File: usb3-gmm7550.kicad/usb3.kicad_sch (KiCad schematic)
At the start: 31 parts, among them J1 USB_C_Receptacle, U1 ECMF4-40A100N10, U2 ECMF4-40A100N10, U3 ECMF02-2AMX6, U4 AP7330, U5 TUSB542

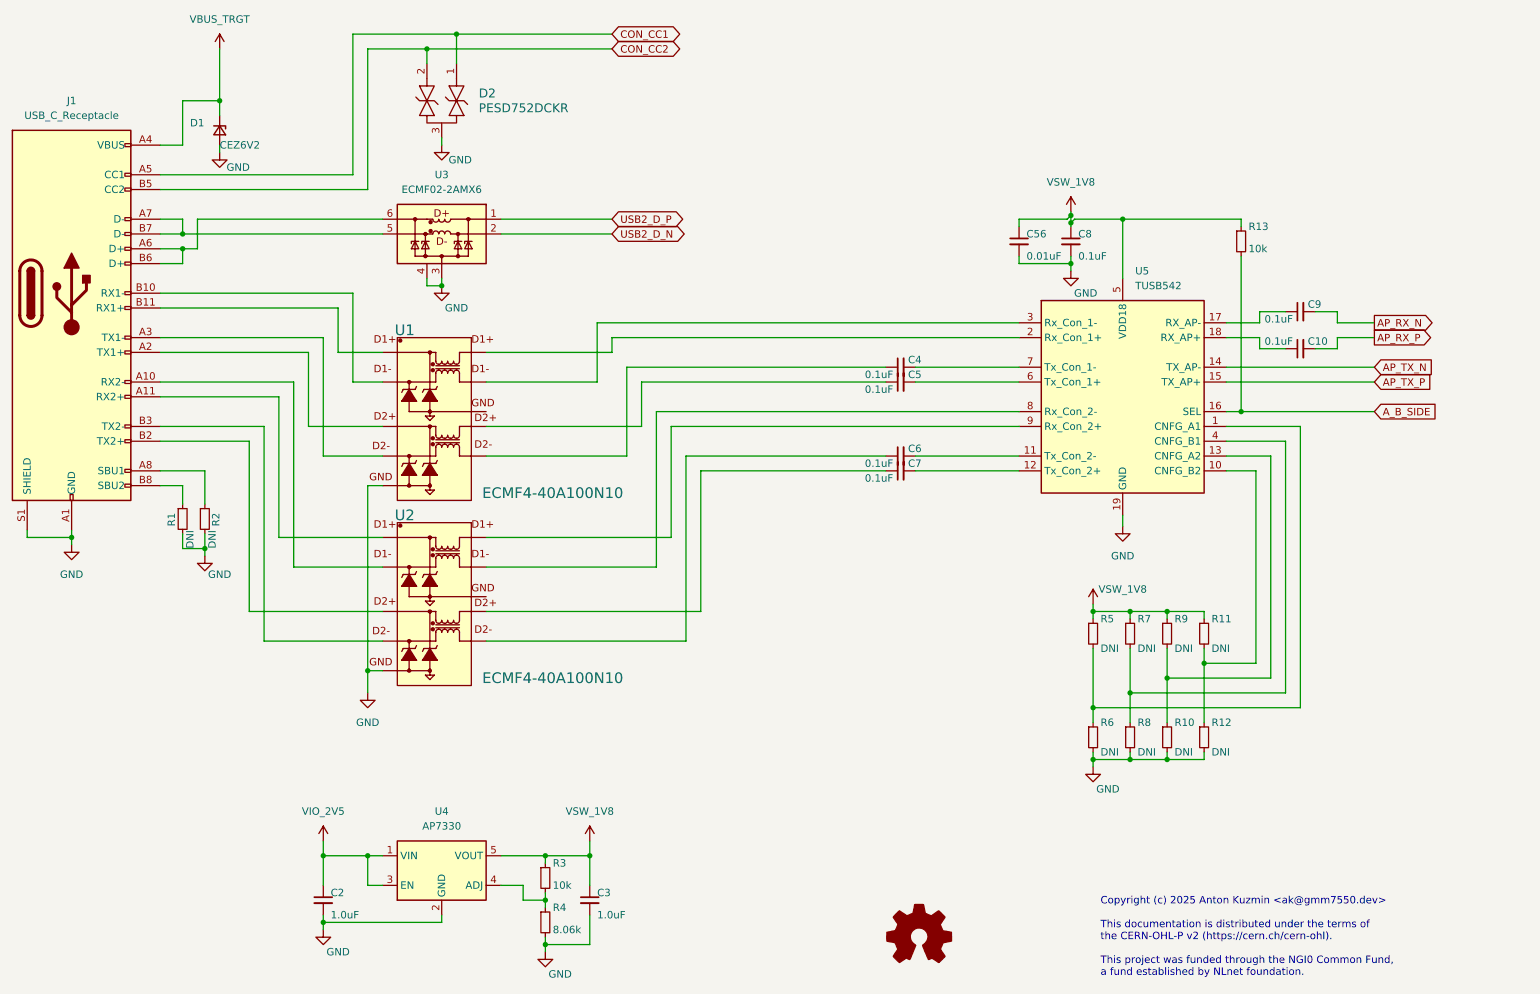
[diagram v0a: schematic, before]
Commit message: Connect USB 3 SuperSpeed diff. pairs
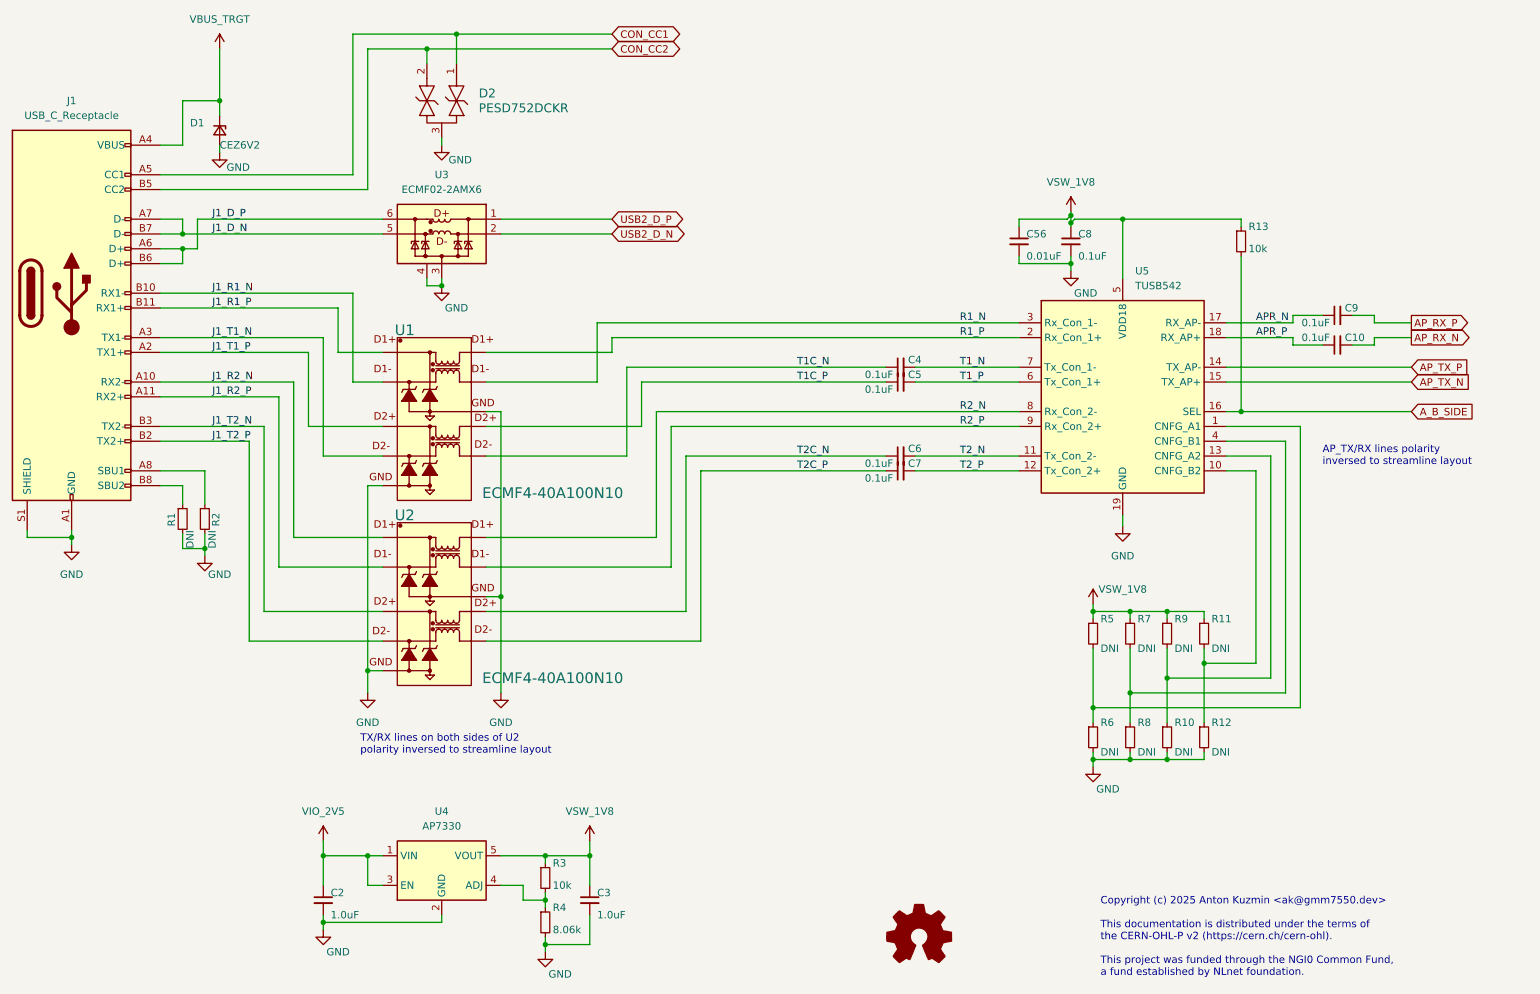
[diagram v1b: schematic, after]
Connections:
- net AP_RX_N: now also C10.2; no longer C9.2
- net AP_RX_P: now also C9.2; no longer C10.2
- net AP_TX_N: now also U5.15 (TX_AP+); no longer U5.14 (TX_AP-)
- net AP_TX_P: now also U5.14 (TX_AP-); no longer U5.15 (TX_AP+)
- net GND: now also U1.8 (GND1), U2.8 (GND1)
- net APR_N: now reaches C9.1, U5.17 (RX_AP-)
- net T1C_N: now reaches C4.1, U1.6 (D2-1)
- net T1_N: now reaches C4.2, U5.7 (Tx_Con_1-)
- net J1_R1_P: now reaches J1.B11 (RX1+), U1.1 (D1+)
- net R1_P: now reaches U1.10 (D1+1), U5.2 (Rx_Con_1+)
- net J1_R1_N: now reaches J1.B10 (RX1-), U1.2 (D1-)
- net J1_T1_P: now reaches J1.A2 (TX1+), U1.4 (D2+)
- net J1_T1_N: now reaches J1.A3 (TX1-), U1.5 (D2-)
- net T1C_P: now reaches C5.1, U1.7 (D2+1)
- net R1_N: now reaches U1.9 (D1-1), U5.3 (Rx_Con_1-)
- net J1_R2_N: now reaches U2.1 (D1+)
- net J1_R2_N: now also J1.A10 (RX2-); no longer J1.A11 (RX2+)
- net R2_N: now reaches U2.10 (D1+1)
- net R2_N: now also U5.8 (Rx_Con_2-); no longer U5.9 (Rx_Con_2+)
- net J1_R2_P: now reaches U2.2 (D1-)
- net J1_R2_P: now also J1.A11 (RX2+); no longer J1.A10 (RX2-)
- net J1_T2_N: now reaches U2.4 (D2+)
- net J1_T2_N: now also J1.B3 (TX2-); no longer J1.B2 (TX2+)
- net J1_T2_P: now reaches U2.5 (D2-)
- net J1_T2_P: now also J1.B2 (TX2+); no longer J1.B3 (TX2-)
- net T2C_N: now reaches C6.1
- net T2C_N: now also U2.7 (D2+1); no longer U2.6 (D2-1)
- net T2C_P: now reaches C7.1
- net T2C_P: now also U2.6 (D2-1); no longer U2.7 (D2+1)
- net R2_P: now reaches U2.9 (D1-1)
- net R2_P: now also U5.9 (Rx_Con_2+); no longer U5.8 (Rx_Con_2-)
- net T2_N: now reaches C6.2, U5.11 (Tx_Con_2-)
- net T2_P: now reaches C7.2, U5.12 (Tx_Con_2+)
- net APR_P: now reaches C10.1, U5.18 (RX_AP+)
- net T1_P: now reaches C5.2, U5.6 (Tx_Con_1+)
- net J1_D_N: now reaches J1.A7 (D-), J1.B7 (D-), U3.5 (D-_out)
- net J1_D_P: now reaches J1.A6 (D+), J1.B6 (D+), U3.6 (D+_out)
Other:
- note added: "AP_TX/RX lines polarity inversed to streamline layout"
- note added: "TX/RX lines on both sides of U2 polarity inversed to streamline layout"
- moved on the sheet: C10, C9

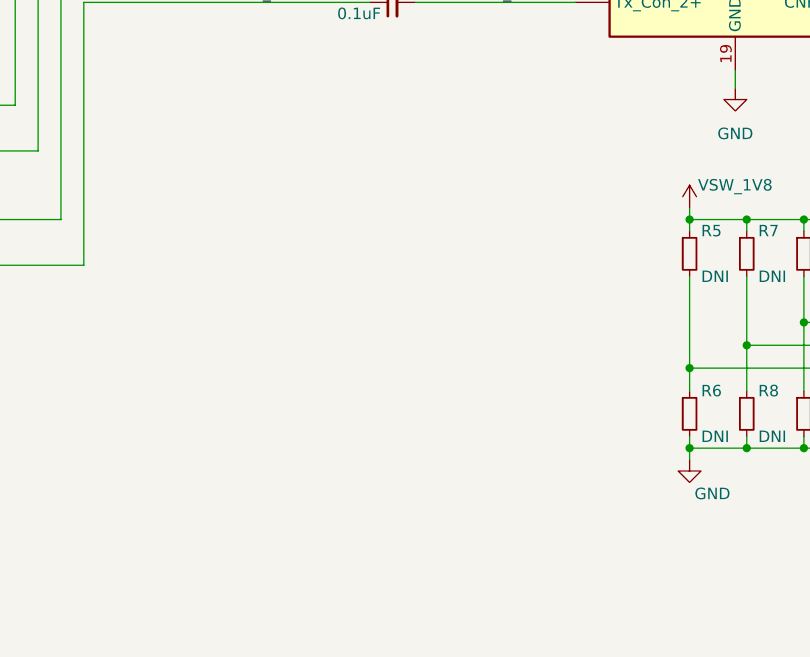
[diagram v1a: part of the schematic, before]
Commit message: Add USB Type-C plug polarity indication (A_B_SIDE signal from PD controller)
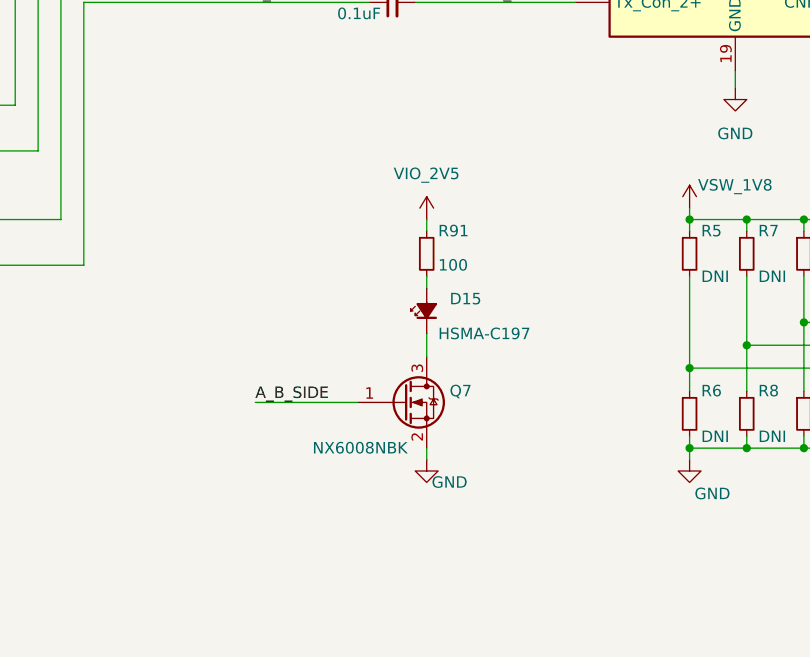
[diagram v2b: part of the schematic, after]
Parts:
- added D15: HSMA-C197, LED_SMD:LED_0603_1608Metric, symbol Device:LED_Small_Filled
- added Q7: NX6008NBK, Package_TO_SOT_SMD:SOT-23, symbol Device:Q_NMOS_GSD
- added R91: 100, Resistor_SMD:R_0402_1005Metric, symbol Device:R_Small
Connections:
- net A_B_SIDE: now also Q7.1 (G)
- net GND: now also Q7.2 (S)
- net VIO_2V5: now also R91.1
- new net: D15.1 (K), Q7.3 (D)
- new net: D15.2 (A), R91.2

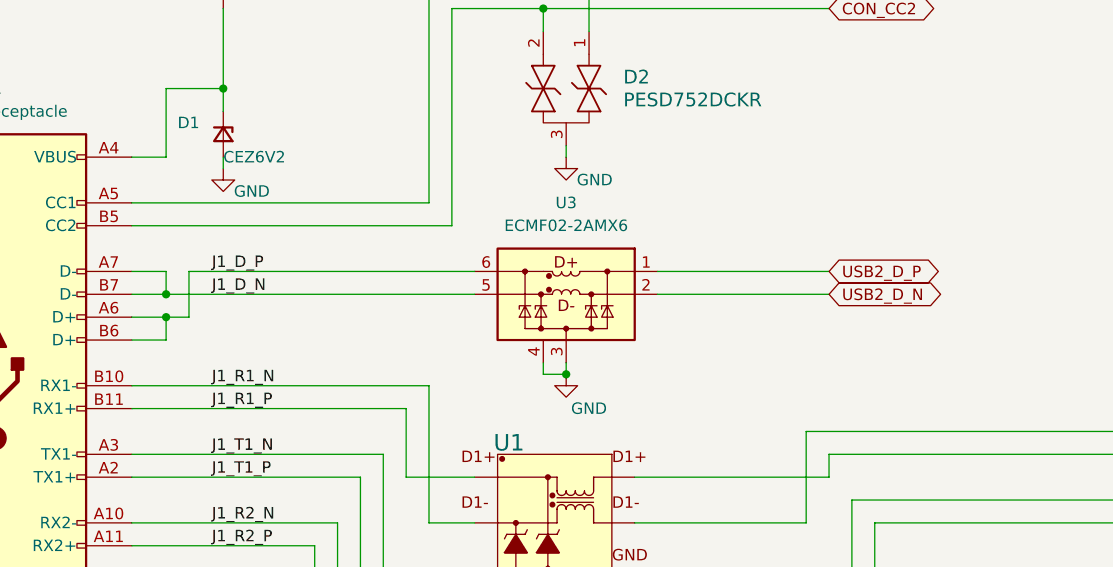
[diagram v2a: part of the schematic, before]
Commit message: Layout -- re-arrange and connect all GMM-7550 IOs on J4 (USB 1.1 and 2.0)
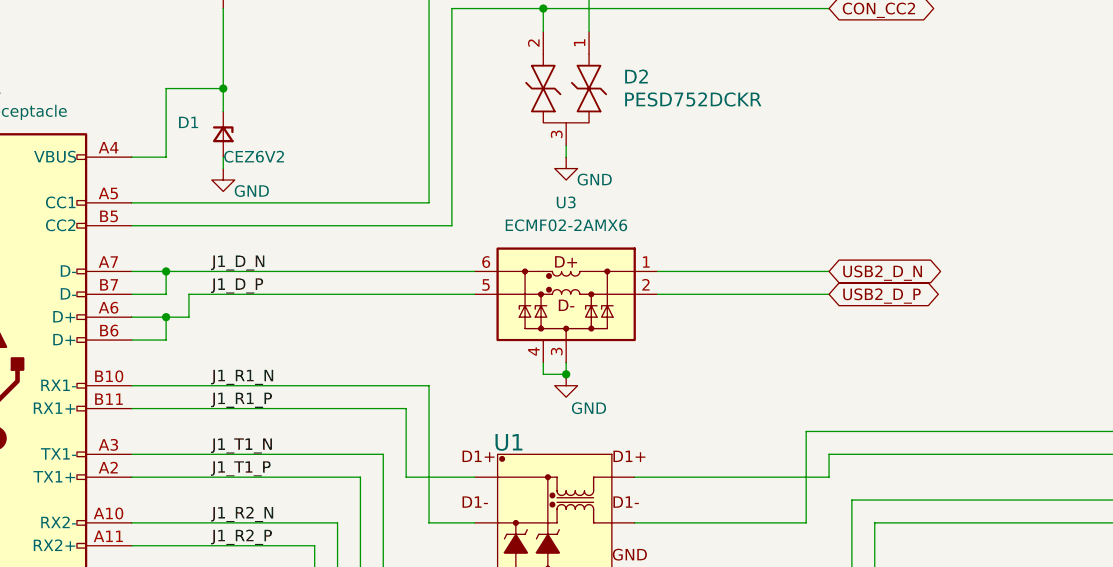
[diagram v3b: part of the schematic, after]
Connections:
- net J1_D_N: now also U3.6 (D+_out); no longer U3.5 (D-_out)
- net J1_D_P: now also U3.5 (D-_out); no longer U3.6 (D+_out)
- net USB2_D_N: now also U3.1 (D+_in); no longer U3.2 (D-_in)
- net USB2_D_P: now also U3.2 (D-_in); no longer U3.1 (D+_in)
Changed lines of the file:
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@@
 	(title_block
 		(title "GMM-7550 USB3 Adapter")
-		(date "2025-09-02")
-		(rev "0.9.3")
+		(date "2025-09-xx")
+		(rev "0.9.4")
 	)
 	(text "Copyright (c) 2025 Anton Kuzmin <ak@gmm7550.dev>\n\nThis documentation is distributed under the terms of\nthe CERN-OHL-P v2 (https://cern.ch/cern-ohl).\n\nThis project was funded through the NGI0 Common Fund,\na fund established by NLnet foundation."
@@
 	)
 	(junction
-		(at 57.15 53.34)
-		(diameter 0)
-		(color 0 0 0 0)
-	)
-	(junction
 		(at 232.41 127)
 		(diameter 0)
@@
 	)
 	(junction
+		(at 57.15 50.8)
+		(diameter 0)
+		(color 0 0 0 0)
+	)
+	(junction
 		(at 226.06 118.11)
 		(diameter 0)
@@
 	(wire
 		(pts
-			(xy 57.15 53.34) (xy 91.44 53.34)
-		)
-		(stroke
-			(width 0)
-			(type default)
-		)
-	)
-	(wire
-		(pts
 			(xy 128.27 78.74) (xy 128.27 68.58)
 		)
@@
 	(wire
 		(pts
-			(xy 111.76 50.8) (xy 130.81 50.8)
-		)
-		(stroke
-			(width 0)
-			(type default)
-		)
-	)
-	(wire
-		(pts
 			(xy 109.22 73.66) (xy 130.81 73.66)
 		)
@@
 	(wire
 		(pts
+			(xy 111.76 50.8) (xy 130.81 50.8)
+		)
+		(stroke
+			(width 0)
+			(type default)
+		)
+	)
+	(wire
+		(pts
 			(xy 236.22 91.44) (xy 243.84 91.44)
 		)
@@
 	(wire
 		(pts
-			(xy 59.69 55.88) (xy 57.15 55.88)
+			(xy 57.15 55.88) (xy 59.69 55.88)
 		)
 		(stroke
@@
 	(wire
 		(pts
-			(xy 111.76 53.34) (xy 130.81 53.34)
-		)
-		(stroke
-			(width 0)
-			(type default)
-		)
-	)
-	(wire
-		(pts
 			(xy 53.34 81.28) (xy 73.66 81.28)
 		)
@@
 	(wire
 		(pts
+			(xy 59.69 55.88) (xy 59.69 53.34)
+		)
+		(stroke
+			(width 0)
+			(type default)
+		)
+	)
+	(wire
+		(pts
 			(xy 60.96 104.775) (xy 60.96 107.315)
 		)
@@
 	(wire
 		(pts
-			(xy 78.74 73.66) (xy 78.74 86.36)
+			(xy 57.15 50.8) (xy 91.44 50.8)
 		)
 		(stroke
@@
 	(wire
 		(pts
-			(xy 86.36 78.74) (xy 91.44 78.74)
+			(xy 78.74 73.66) (xy 78.74 86.36)
 		)
 		(stroke
@@
 	(wire
 		(pts
-			(xy 99.06 60.96) (xy 99.06 62.23)
+			(xy 86.36 78.74) (xy 91.44 78.74)
 		)
 		(stroke
@@
 	(wire
 		(pts
-			(xy 88.9 165.1) (xy 88.9 160.02)
+			(xy 99.06 60.96) (xy 99.06 62.23)
 		)
 		(stroke
@@
 	(wire
 		(pts
-			(xy 53.34 53.34) (xy 57.15 53.34)
+			(xy 88.9 165.1) (xy 88.9 160.02)
 		)
 		(stroke
@@
 	(wire
 		(pts
-			(xy 182.88 78.74) (xy 200.66 78.74)
+			(xy 53.34 53.34) (xy 57.15 53.34)
 		)
 		(stroke
@@
 	(wire
 		(pts
-			(xy 209.55 51.435) (xy 209.55 52.07)
+			(xy 182.88 78.74) (xy 200.66 78.74)
 		)
 		(stroke
@@
 	(wire
 		(pts
-			(xy 59.69 50.8) (xy 59.69 55.88)
+			(xy 209.55 51.435) (xy 209.55 52.07)
 		)
 		(stroke
@@
 	(wire
 		(pts
+			(xy 59.69 53.34) (xy 91.44 53.34)
+		)
+		(stroke
+			(width 0)
+			(type default)
+		)
+	)
+	(wire
+		(pts
 			(xy 209.55 58.42) (xy 209.55 59.69)
 		)
@@
 	(wire
 		(pts
+			(xy 111.76 53.34) (xy 130.81 53.34)
+		)
+		(stroke
+			(width 0)
+			(type default)
+		)
+	)
+	(wire
+		(pts
 			(xy 210.185 50.8) (xy 209.55 51.435)
 		)
@@
 	(wire
 		(pts
-			(xy 91.44 50.8) (xy 59.69 50.8)
-		)
-		(stroke
-			(width 0)
-			(type default)
-		)
-	)
-	(wire
-		(pts
 			(xy 236.22 78.74) (xy 267.97 78.74)
 		)
@@
 	)
 	(label "J1_D_N"
-		(at 62.23 53.34 0)
+		(at 62.23 50.8 0)
 		(effects
 			(font
@@
 	)
 	(label "J1_D_P"
-		(at 62.23 50.8 0)
+		(at 62.23 53.34 0)
 		(effects
 			(font
@@
 	(global_label "USB2_D_N"
 		(shape bidirectional)
-		(at 130.81 53.34 0)
+		(at 130.81 50.8 0)
 		(fields_autoplaced yes)
 		(effects
@@
 		)
 		(property "Intersheetrefs" "${INTERSHEET_REFS}"
-			(at 144.4617 53.34 0)
+			(at 144.4617 50.8 0)
 			(effects
 				(font
@@
 	(global_label "USB2_D_P"
 		(shape bidirectional)
-		(at 130.81 50.8 0)
+		(at 130.81 53.34 0)
 		(fields_autoplaced yes)
 		(effects
@@
 		)
 		(property "Intersheetrefs" "${INTERSHEET_REFS}"
-			(at 144.4012 50.8 0)
+			(at 144.4012 53.34 0)
 			(effects
 				(font

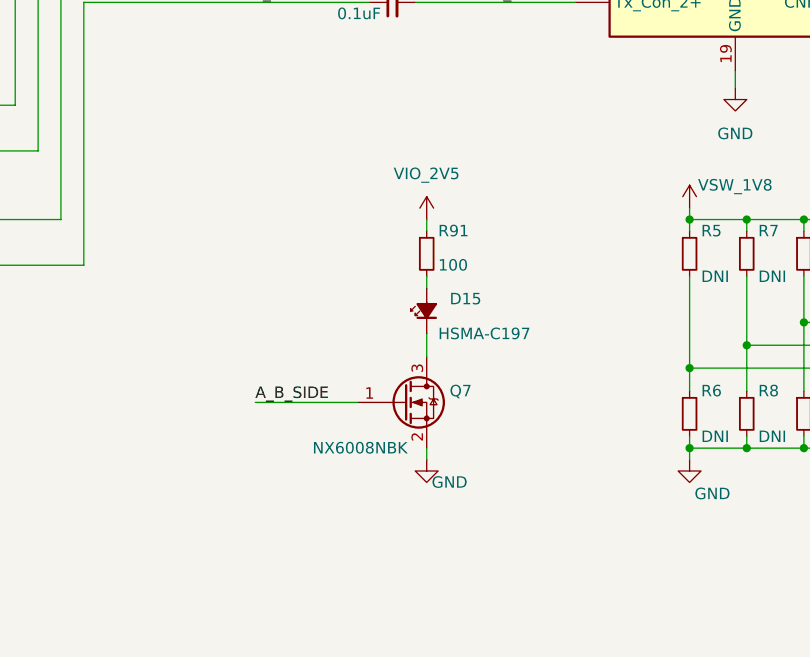
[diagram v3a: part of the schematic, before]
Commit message: USB Power Delivery redesign (STmicro controller is NRND)
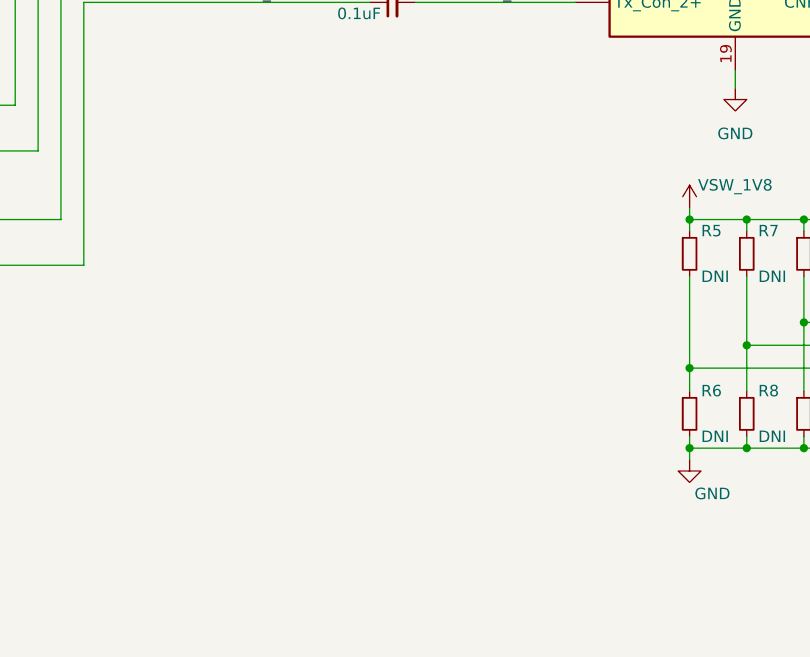
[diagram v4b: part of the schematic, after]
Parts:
- removed D15: HSMA-C197, LED_SMD:LED_0603_1608Metric, symbol Device:LED_Small_Filled
- removed Q7: NX6008NBK, Package_TO_SOT_SMD:SOT-23, symbol Device:Q_NMOS_GSD
- removed R91: 100, Resistor_SMD:R_0402_1005Metric, symbol Device:R_Small

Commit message: Layout WIP: split power plane (internal layer 2)
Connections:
- net CON_CC1: now also D2.2; no longer D2.1
- net CON_CC2: now also D2.1; no longer D2.2
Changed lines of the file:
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@@
+	)
+	(junction
+		(at 104.14 21.59)
+		(diameter 0)
+		(color 0 0 0 0)
 	)
 	(junction
@@
 	)
 	(junction
-		(at 104.14 19.05)
-		(diameter 0)
-		(color 0 0 0 0)
-	)
-	(junction
 		(at 111.76 115.57)
 		(diameter 0)
@@
 	)
 	(junction
-		(at 99.06 21.59)
-		(diameter 0)
-		(color 0 0 0 0)
-	)
-	(junction
 		(at 238.76 83.82)
 		(diameter 0)
@@
 	)
 	(junction
+		(at 99.06 19.05)
+		(diameter 0)
+		(color 0 0 0 0)
+	)
+	(junction
 		(at 57.15 55.88)
 		(diameter 0)
@@
 	(wire
 		(pts
+			(xy 104.14 21.59) (xy 130.81 21.59)
+		)
+		(stroke
+			(width 0)
+			(type default)
+		)
+	)
+	(wire
+		(pts
 			(xy 109.22 118.11) (xy 143.51 118.11)
 		)
@@
 	(wire
 		(pts
-			(xy 99.06 21.59) (xy 99.06 24.13)
-		)
-		(stroke
-			(width 0)
-			(type default)
-		)
-	)
-	(wire
-		(pts
 			(xy 238.76 52.07) (xy 238.76 50.8)
 		)
@@
 	(wire
 		(pts
+			(xy 99.06 19.05) (xy 130.81 19.05)
+		)
+		(stroke
+			(width 0)
+			(type default)
+		)
+	)
+	(wire
+		(pts
 			(xy 200.66 52.07) (xy 200.66 50.8)
 		)
@@
 	(wire
 		(pts
-			(xy 104.14 19.05) (xy 104.14 24.13)
-		)
-		(stroke
-			(width 0)
-			(type default)
-		)
-	)
-	(wire
-		(pts
 			(xy 213.36 124.46) (xy 213.36 134.62)
 		)
@@
 	(wire
 		(pts
-			(xy 99.06 21.59) (xy 130.81 21.59)
+			(xy 88.9 21.59) (xy 104.14 21.59)
+		)
+		(stroke
+			(width 0)
+			(type default)
+		)
+	)
+	(wire
+		(pts
+			(xy 99.06 19.05) (xy 99.06 24.13)
 		)
 		(stroke
@@
 	(wire
 		(pts
-			(xy 104.14 19.05) (xy 130.81 19.05)
-		)
-		(stroke
-			(width 0)
-			(type default)
-		)
-	)
-	(wire
-		(pts
 			(xy 57.15 55.88) (xy 59.69 55.88)
 		)
@@
 	(wire
 		(pts
-			(xy 88.9 21.59) (xy 99.06 21.59)
-		)
-		(stroke
-			(width 0)
-			(type default)
-		)
-	)
-	(wire
-		(pts
 			(xy 261.62 71.12) (xy 267.97 71.12)
 		)
@@
 	(wire
 		(pts
-			(xy 86.36 19.05) (xy 104.14 19.05)
+			(xy 86.36 19.05) (xy 99.06 19.05)
 		)
 		(stroke
@@
 		)
 		(stroke
+			(width 0)
+			(type default)
+		)
+	)
+	(wire
+		(pts
+			(xy 104.14 21.59) (xy 104.14 24.13)
+		)
+		(stroke
